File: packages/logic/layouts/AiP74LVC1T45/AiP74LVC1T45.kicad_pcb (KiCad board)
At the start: 2 copper layers, 3 parts

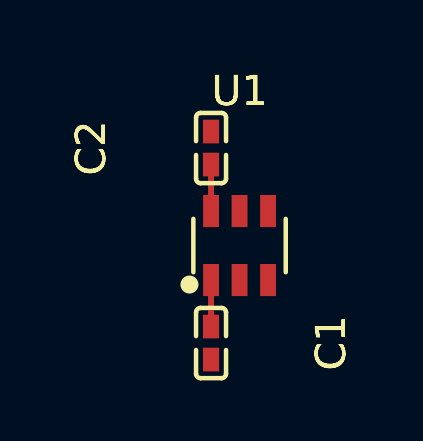
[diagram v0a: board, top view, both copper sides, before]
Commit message: Build all packages without designators on silkscreen.
Also disable fail_on_drc and enable keep_picked_parts for build
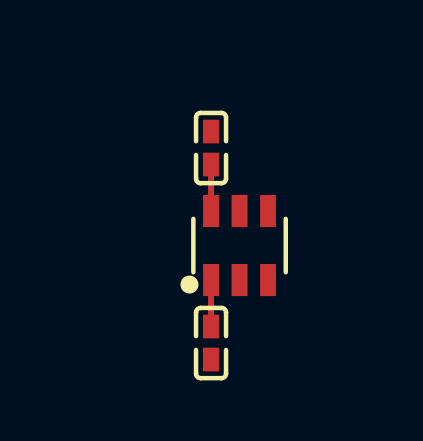
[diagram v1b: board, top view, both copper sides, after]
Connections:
- C1 pad 1: hv -> hv-1
- C2 pad 1: hv-1 -> hv
- U1 pad 1: hv -> hv-1
- U1 pad 3: buffer-line-1 -> buffer-line-2
- U1 pad 5: buffer-line-2 -> buffer-line-1
- U1 pad 6: hv-1 -> hv
